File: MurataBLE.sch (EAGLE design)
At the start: 58 parts, among them CON1 47589-0001, IC2 LPC11U35_QFN33, IC3 NC7SZ00, IC4 AT25DN512C, IC5 AT25XE011, P1 NC, P2 NC, P3 NC, P4 NC, Q1 32.768K/2012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

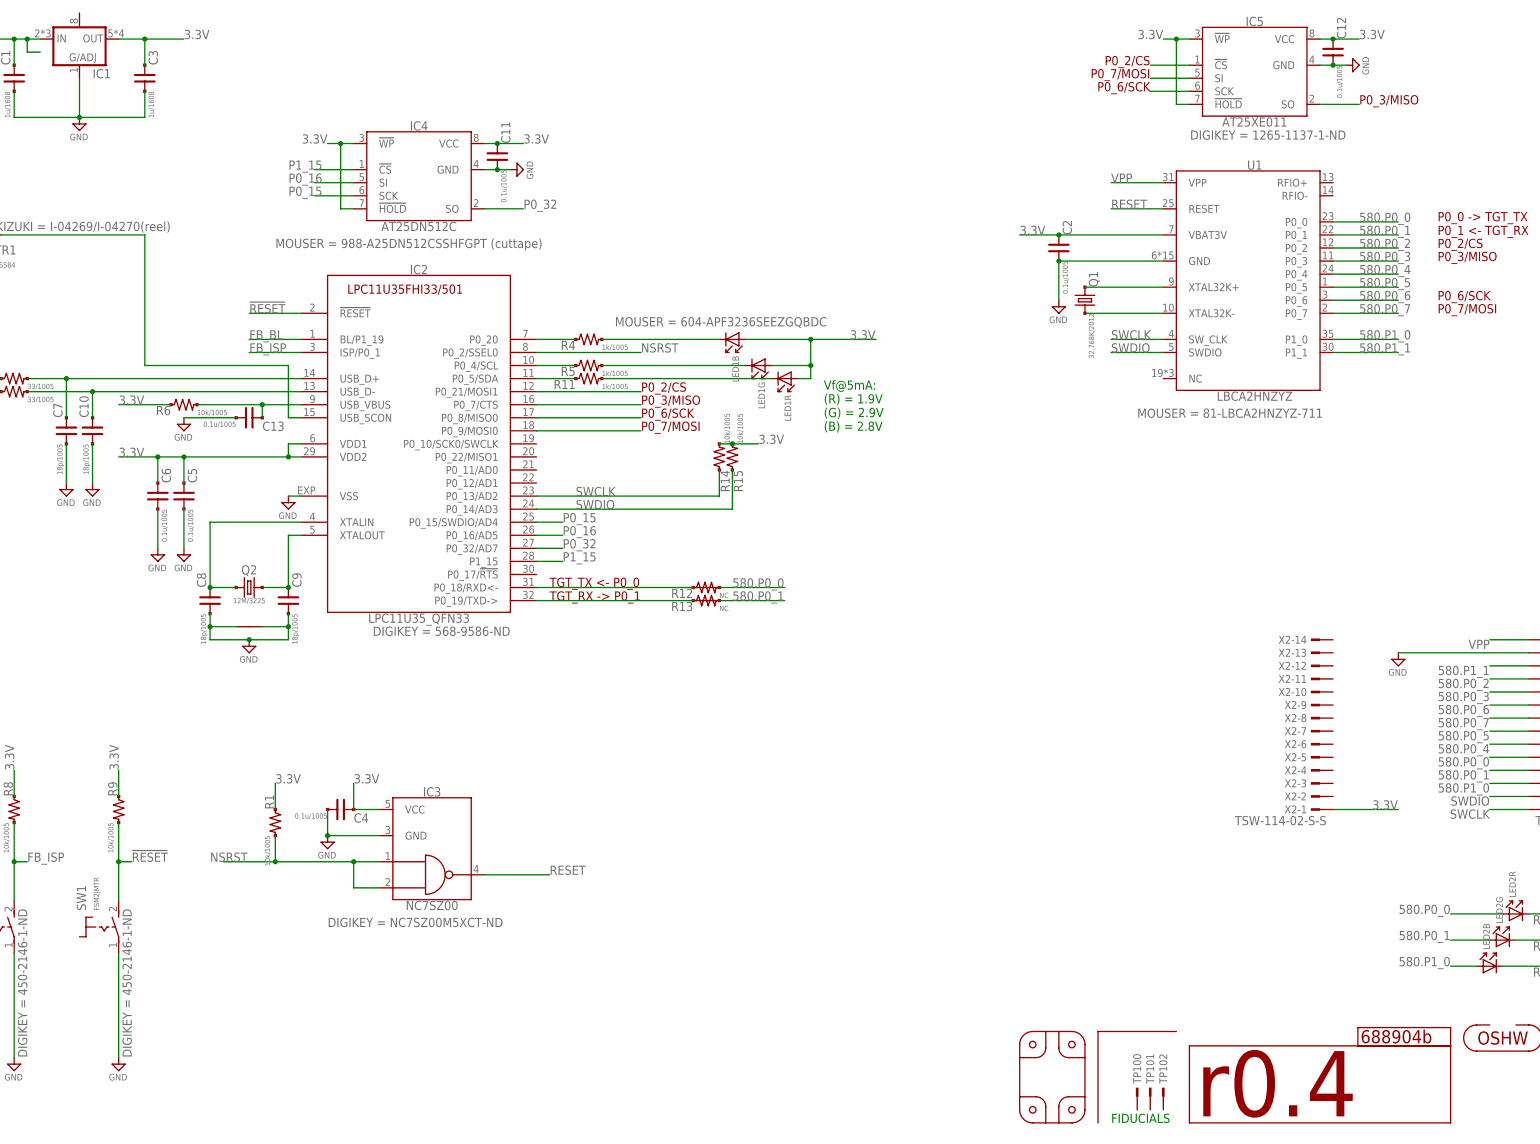
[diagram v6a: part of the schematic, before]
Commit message: [ USB ] IC1 has value
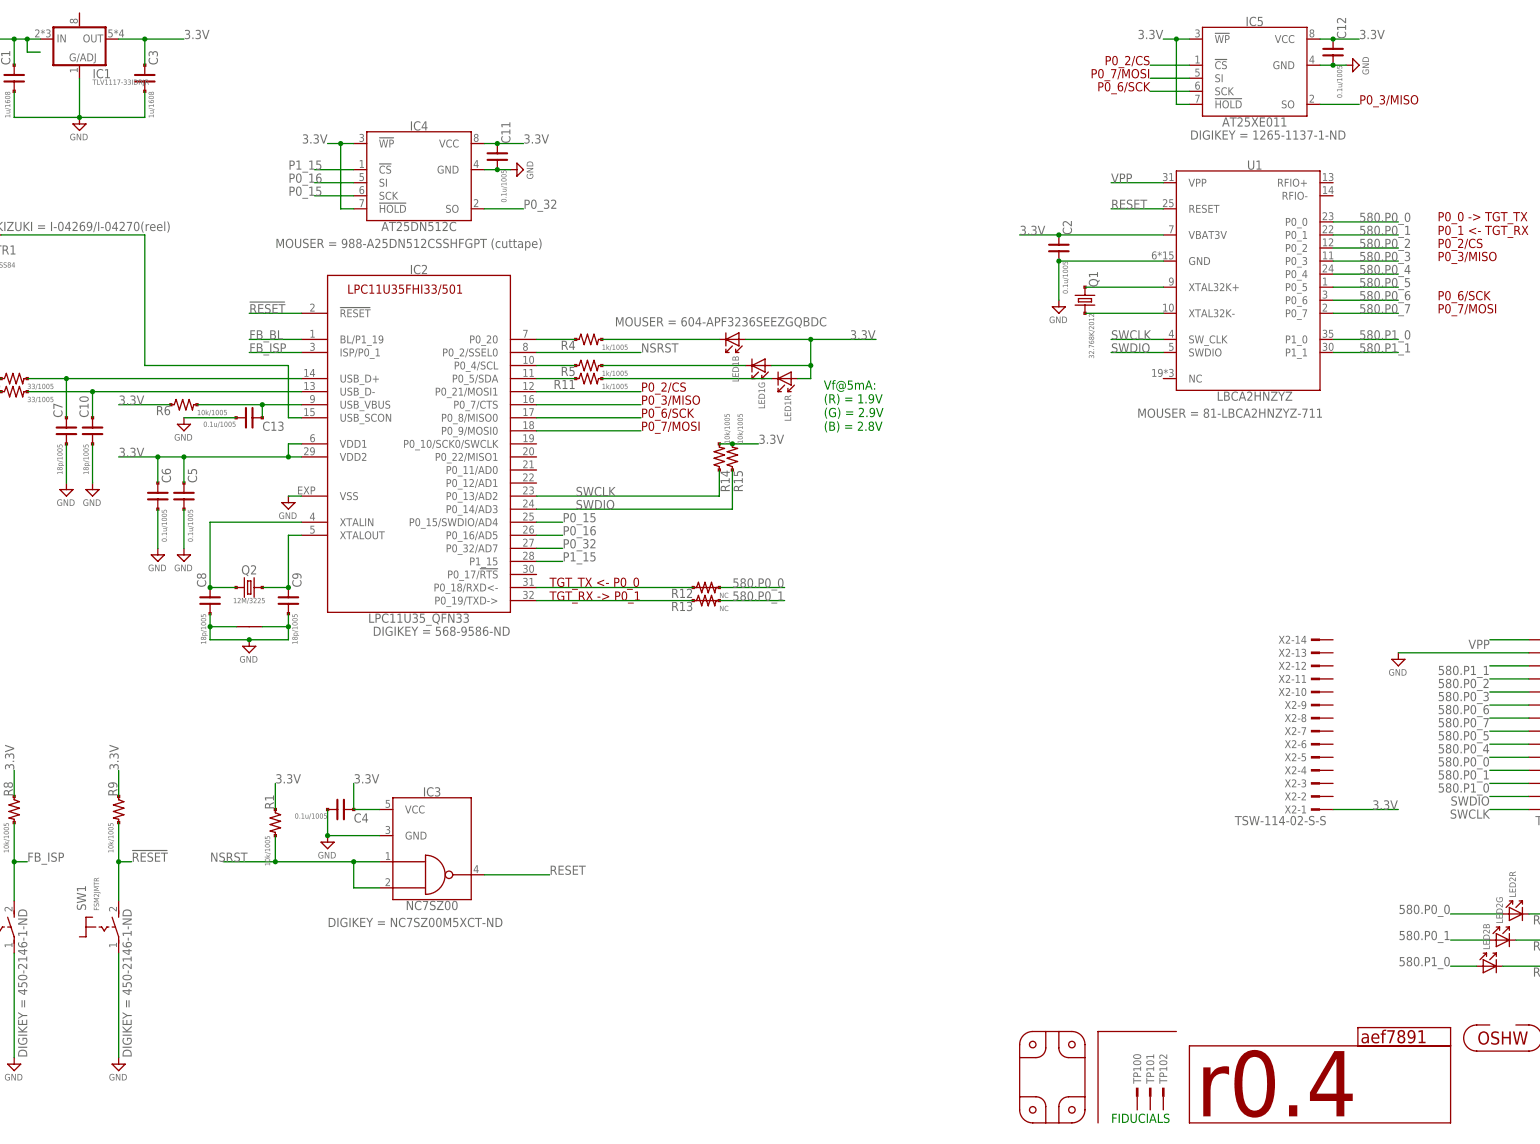
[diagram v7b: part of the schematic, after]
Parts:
- GIT1: value 688904b -> aef7891
- IC1: value (none) -> TLV1117-33IDRJR
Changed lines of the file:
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@@
 <part name="R13" library="mylib" deviceset="R_US_*" device="_1005SHORT" value="NC"/>
 <part name="IC3" library="mylib" deviceset="IC_TTL_SINGLE_74_00" device="_SOT23" value="NC7SZ00"/>
-<part name="GIT1" library="git-revision" deviceset="GIT-REVISION" device="" value="688904b"/>
+<part name="GIT1" library="git-revision" deviceset="GIT-REVISION" device="" value="aef7891"/>
 <part name="X2" library="mylib" deviceset="TSW-114-02-S-S" device="" value="TSW-114-02-S-S">
 <attribute name="NOT_COMPONENT" value="YES"/>
@@
 <part name="SUPPLY7" library="mylib" deviceset="GND" device=""/>
 <part name="SUPPLY16" library="mylib" deviceset="GND" device=""/>
-<part name="IC1" library="mylib" deviceset="LDO4_*" device="_DRJ" technology="3.3"/>
+<part name="IC1" library="mylib" deviceset="LDO4_*" device="_DRJ" technology="3.3" value="TLV1117-33IDRJR"/>
 </parts>
 <sheets>

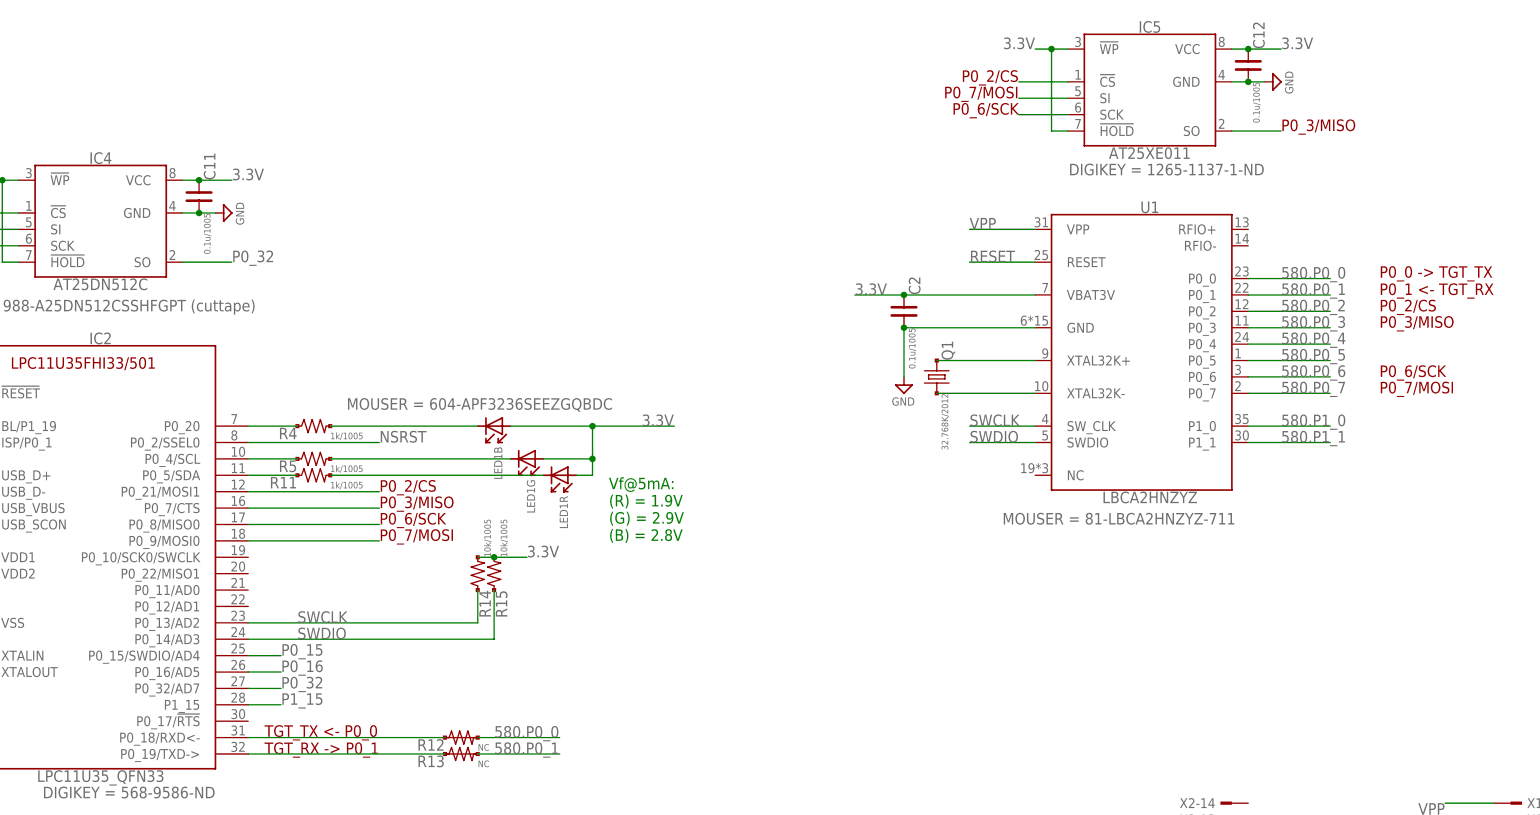
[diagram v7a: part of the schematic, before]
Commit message: [ r0.4 ] update library
typo fix: P0_32 -> P0_23;
add 11U35 PinNames for SPI flash
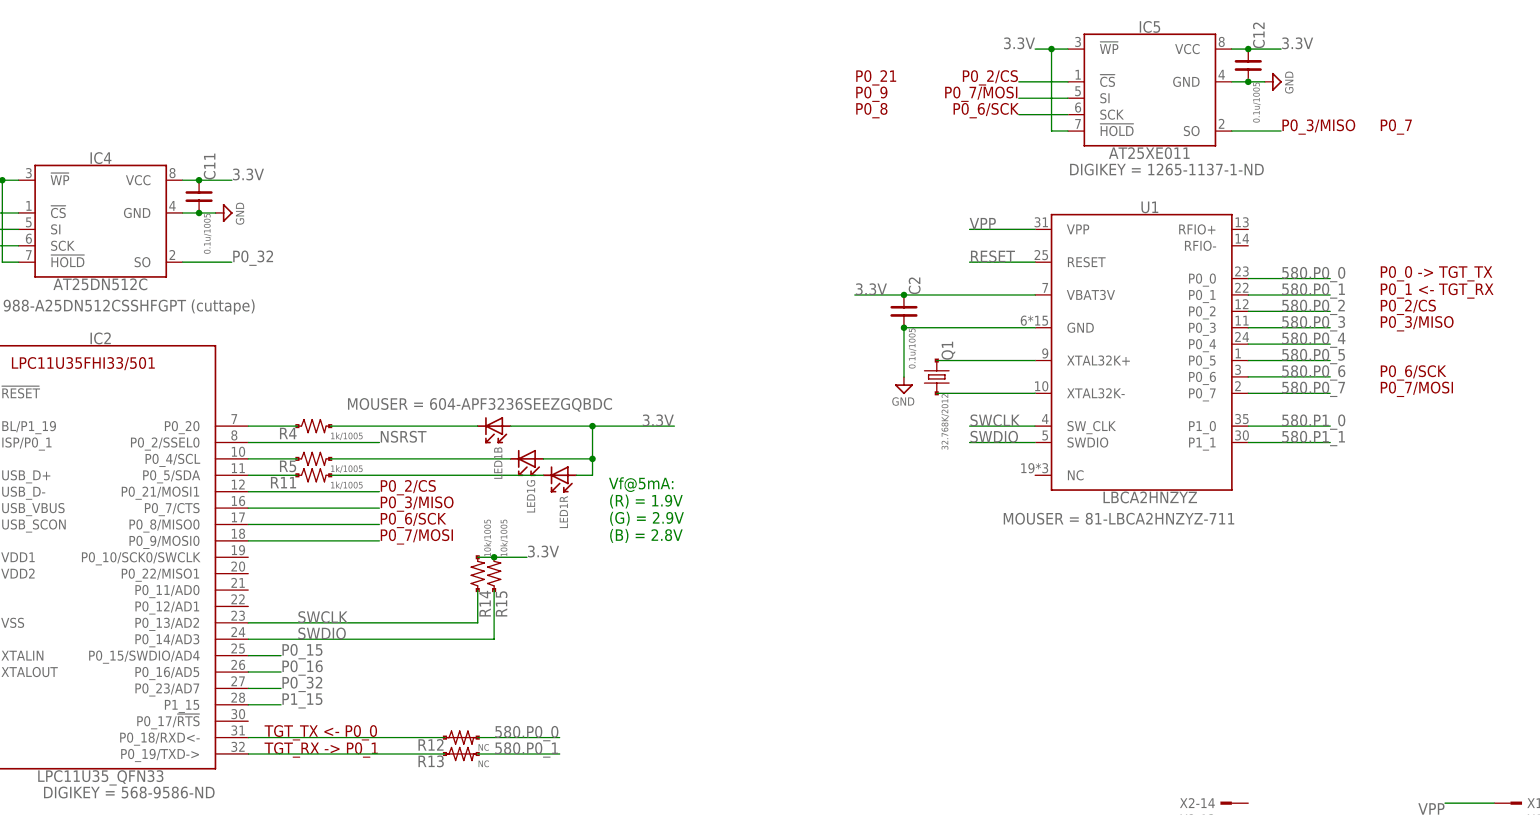
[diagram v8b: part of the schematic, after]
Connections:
- net P0_32: now also IC2.P0_23/AD7; no longer IC2.P0_32/AD7
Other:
- note added: "P0_21"
- note added: "P0_7"
- note added: "P0_8"
- note added: "P0_9"
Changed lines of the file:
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@@
 <text x="337.82" y="162.56" size="1.778" layer="94">P0_7/MOSI</text>
 <text x="337.82" y="165.1" size="1.778" layer="94">P0_6/SCK</text>
+<text x="256.54" y="210.82" size="1.778" layer="94">P0_21</text>
+<text x="256.54" y="208.28" size="1.778" layer="94">P0_9</text>
+<text x="256.54" y="205.74" size="1.778" layer="94">P0_8</text>
+<text x="337.82" y="203.2" size="1.778" layer="94">P0_7</text>
 </plain>
 <instances>
@@
 <net name="P0_32" class="0">
 <segment>
-<pinref part="IC2" gate="G$1" pin="P0_32/AD7"/>
+<pinref part="IC2" gate="G$1" pin="P0_23/AD7"/>
 <wire x1="162.56" y1="116.84" x2="167.64" y2="116.84" width="0.1524" layer="91"/>
 <label x="167.64" y="116.84" size="1.778" layer="95"/>
